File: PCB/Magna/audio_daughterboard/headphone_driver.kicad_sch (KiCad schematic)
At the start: 41 parts, among them J1201 AudioJack3, U1201 NE5532, U1202 NE5532, U1203 TDA2822D

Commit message: Some updates to PCB
Honestly I cannot remember whats changed
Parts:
- renumbered C1201 to C601, C1202 to C602, C1203 to C603, C1204 to C604, C1205 to C605, C1206 to C606, C1207 to C607, C1208 to C608, C1209 to C609, C1210 to C610, C1211 to C611, C1212 to C612, C1213 to C613, C1214 to C614, C1215 to C615, C1216 to C616, C1217 to C617, J1201 to J601, R1201 to R601, R1202 to R602, R1203 to R603, R1204 to R604, R1205 to R605, R1206 to R606, R1207 to R607, R1208 to R608, R1209 to R609, R1210 to R610, R1211 to R611, R1212 to R612, R1213 to R613, R1214 to R614, RV1201 to RV601, TP1201 to TP601, TP1202 to TP602, TP1203 to TP603, TP1204 to TP604, TP1205 to TP605, U1201 to U601, U1202 to U602, U1203 to U603

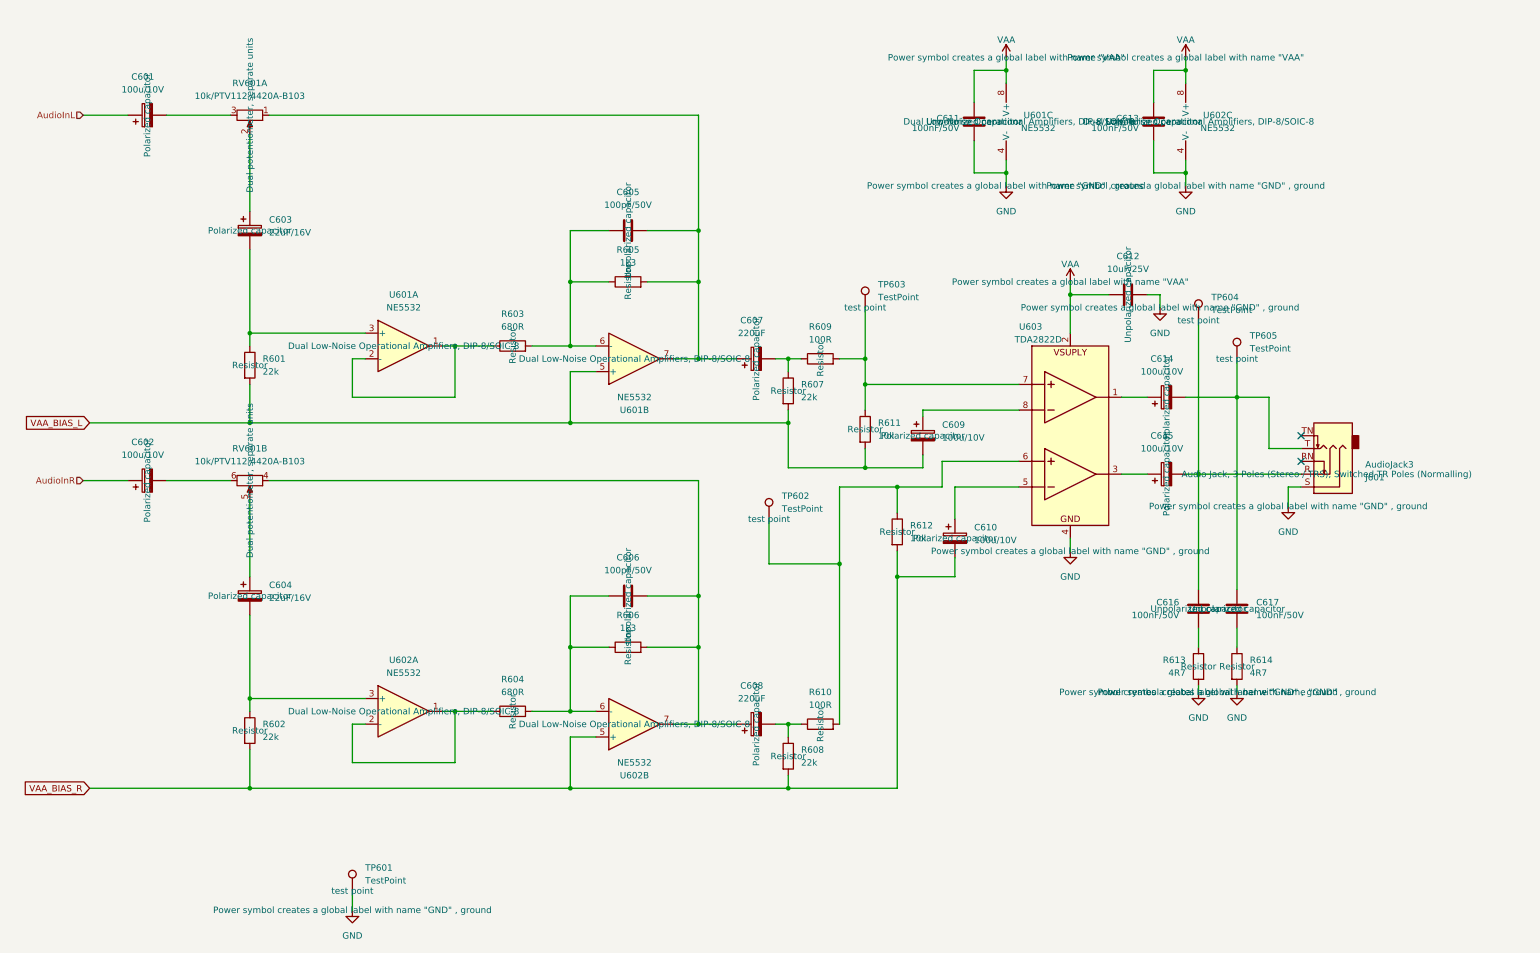
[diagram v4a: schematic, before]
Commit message: Update schematics to Kicad 9
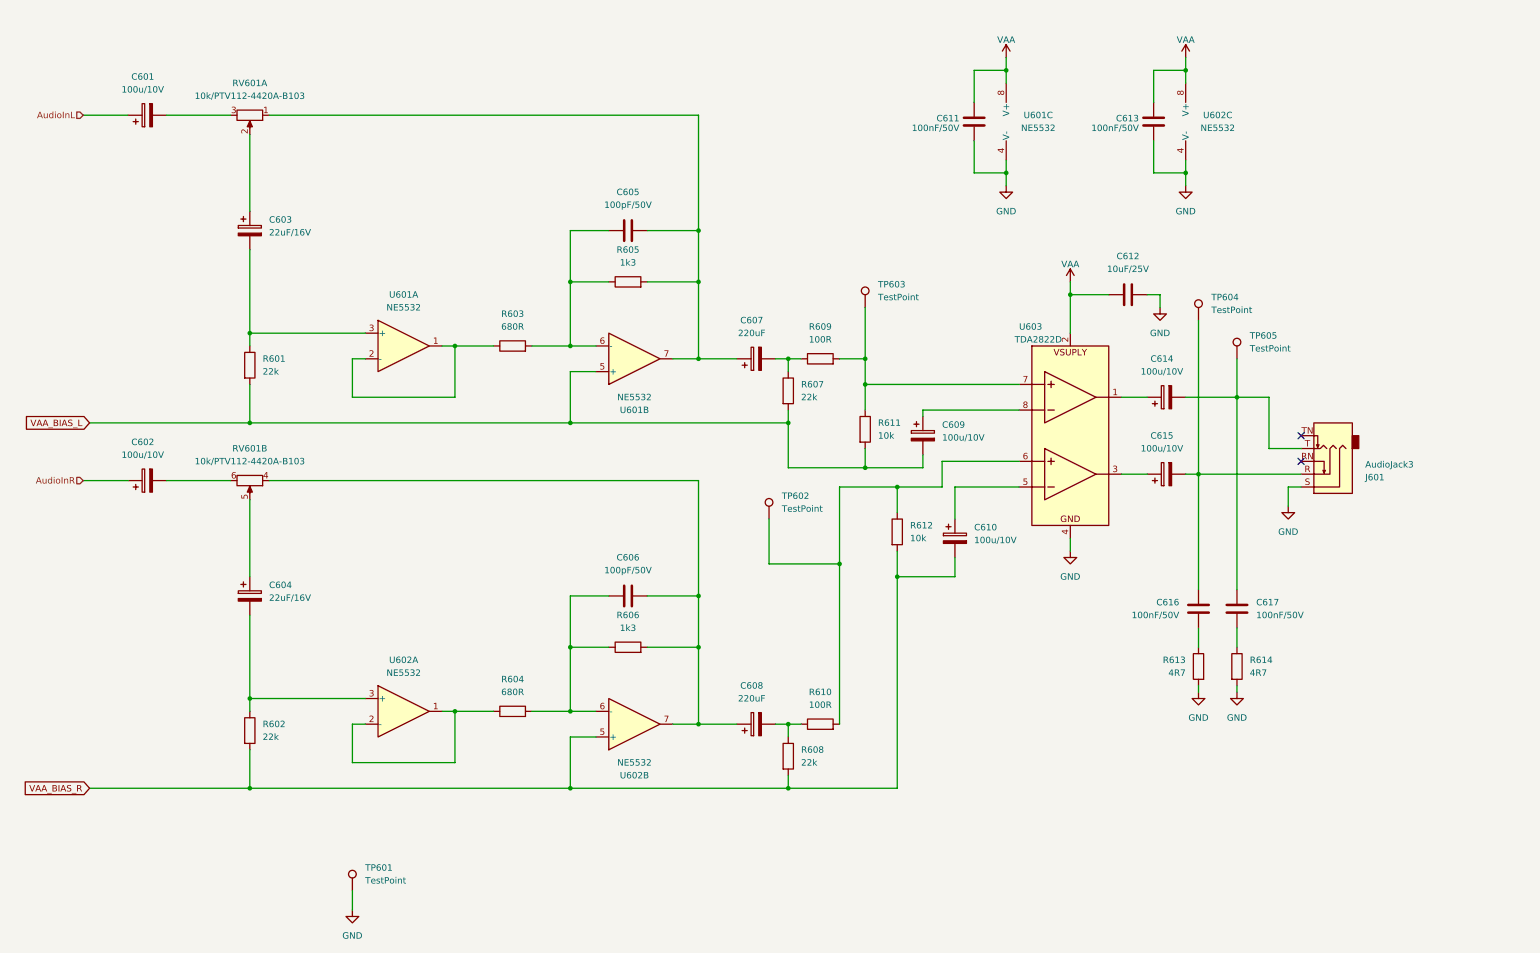
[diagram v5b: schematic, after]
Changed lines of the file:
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@@
 					(size 1.27 1.27)
 				)
+				(hide yes)
 			)
 		)
@@
 					(size 1.27 1.27)
 				)
+				(hide yes)
 			)
 		)
@@
 					(size 1.27 1.27)
 				)
+				(hide yes)
 			)
 		)
@@
 					(size 1.27 1.27)
 				)
+				(hide yes)
 			)
 		)
@@
 					(size 1.27 1.27)
 				)
+				(hide yes)
 			)
 		)
@@
 					(size 1.27 1.27)
 				)
+				(hide yes)
 			)
 		)
@@
 					(size 1.27 1.27)
 				)
+				(hide yes)
 			)
 		)
@@
 					(size 1.27 1.27)
 				)
+				(hide yes)
 			)
 		)
@@
 					(size 1.27 1.27)
 				)
+				(hide yes)
 			)
 		)
@@
 					(size 1.27 1.27)
 				)
+				(hide yes)
 			)
 		)
@@
 					(size 1.27 1.27)
 				)
+				(hide yes)
 			)
 		)
@@
 					(size 1.27 1.27)
 				)
+				(hide yes)
 			)
 		)
@@
 					(size 1.27 1.27)
 				)
+				(hide yes)
 			)
 		)
@@
 					(size 1.27 1.27)
 				)
+				(hide yes)
 			)
 		)
@@
 					(size 1.27 1.27)
 				)
+				(hide yes)
 			)
 		)
@@
 					(size 1.27 1.27)
 				)
+				(hide yes)
 			)
 		)
@@
 					(size 1.27 1.27)
 				)
+				(hide yes)
 			)
 		)
@@
 					(size 1.27 1.27)
 				)
+				(hide yes)
 			)
 		)
@@
 					(size 1.27 1.27)
 				)
+				(hide yes)
 			)
 		)
@@
 					(size 1.27 1.27)
 				)
+				(hide yes)
 			)
 		)
@@
 					(size 1.27 1.27)
 				)
+				(hide yes)
 			)
 		)
@@
 					(size 1.27 1.27)
 				)
+				(hide yes)
 			)
 		)
@@
 					(size 1.27 1.27)
 				)
+				(hide yes)
 			)
 		)
@@
 					(size 1.27 1.27)
 				)
+				(hide yes)
 			)
 		)
@@
 					(size 1.27 1.27)
 				)
+				(hide yes)
 			)
 		)
@@
 					(size 1.27 1.27)
 				)
+				(hide yes)
 			)
 		)
@@
 					(size 1.27 1.27)
 				)
+				(hide yes)
 			)
 		)
@@
 					(size 1.27 1.27)
 				)
+				(hide yes)
 			)
 		)
@@
 					(size 1.27 1.27)
 				)
+				(hide yes)
 			)
 		)
@@
 					(size 1.27 1.27)
 				)
+				(hide yes)
 			)
 		)
@@
 					(size 1.27 1.27)
 				)
+				(hide yes)
 			)
 		)
@@
 					(size 1.27 1.27)
 				)
+				(hide yes)
 			)
 		)
@@
 					(size 1.27 1.27)
 				)
+				(hide yes)
 			)
 		)
@@
 					(size 1.27 1.27)
 				)
+				(hide yes)
 			)
 		)
@@
 					(size 1.27 1.27)
 				)
+				(hide yes)
 			)
 		)
@@
 					(size 1.27 1.27)
 				)
+				(hide yes)
 			)
 		)
@@
 					(size 1.27 1.27)
 				)
+				(hide yes)
 			)
 		)
@@
 					(size 1.27 1.27)
 				)
+				(hide yes)
 			)
 		)
@@
 					(size 1.27 1.27)
 				)
+				(hide yes)
 			)
 		)
@@
 					(size 1.27 1.27)
 				)
+				(hide yes)
 			)
 		)
@@
 					(size 1.27 1.27)
 				)
+				(hide yes)
 			)
 		)
@@
 					(size 1.27 1.27)
 				)
+				(hide yes)
 			)
 		)
@@
 					(size 1.27 1.27)
 				)
+				(hide yes)
 			)
 		)
@@
 					(size 1.27 1.27)
 				)
+				(hide yes)
 			)
 		)
@@
 					(size 1.27 1.27)
 				)
+				(hide yes)
 			)
 		)
@@
 					(size 1.27 1.27)
 				)
+				(hide yes)
 			)
 		)
@@
 					(size 1.27 1.27)
 				)
+				(hide yes)
 			)
 		)
@@
 					(size 1.27 1.27)
 				)
+				(hide yes)
 			)
 		)
@@
 					(size 1.27 1.27)
 				)
+				(hide yes)
 			)
 		)
@@
 					(size 1.27 1.27)
 				)
+				(hide yes)
 			)
 		)
@@
 					(size 1.27 1.27)
 				)
+				(hide yes)
 			)
 		)
@@
 					(size 1.27 1.27)
 				)
+				(hide yes)
 			)
 		)
@@
 					(size 1.27 1.27)
 				)
+				(hide yes)
 			)
 		)
@@
 					(size 1.27 1.27)
 				)
+				(hide yes)
 			)
 		)
@@
 					(size 1.27 1.27)
 				)
+				(hide yes)
 			)
 		)
@@
 					(size 1.27 1.27)
 				)
+				(hide yes)
 			)
 		)

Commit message: Update audio PCB
Mainly added simulations to Linedriver and DAC.

Also fixed some small issues that was found when simulating
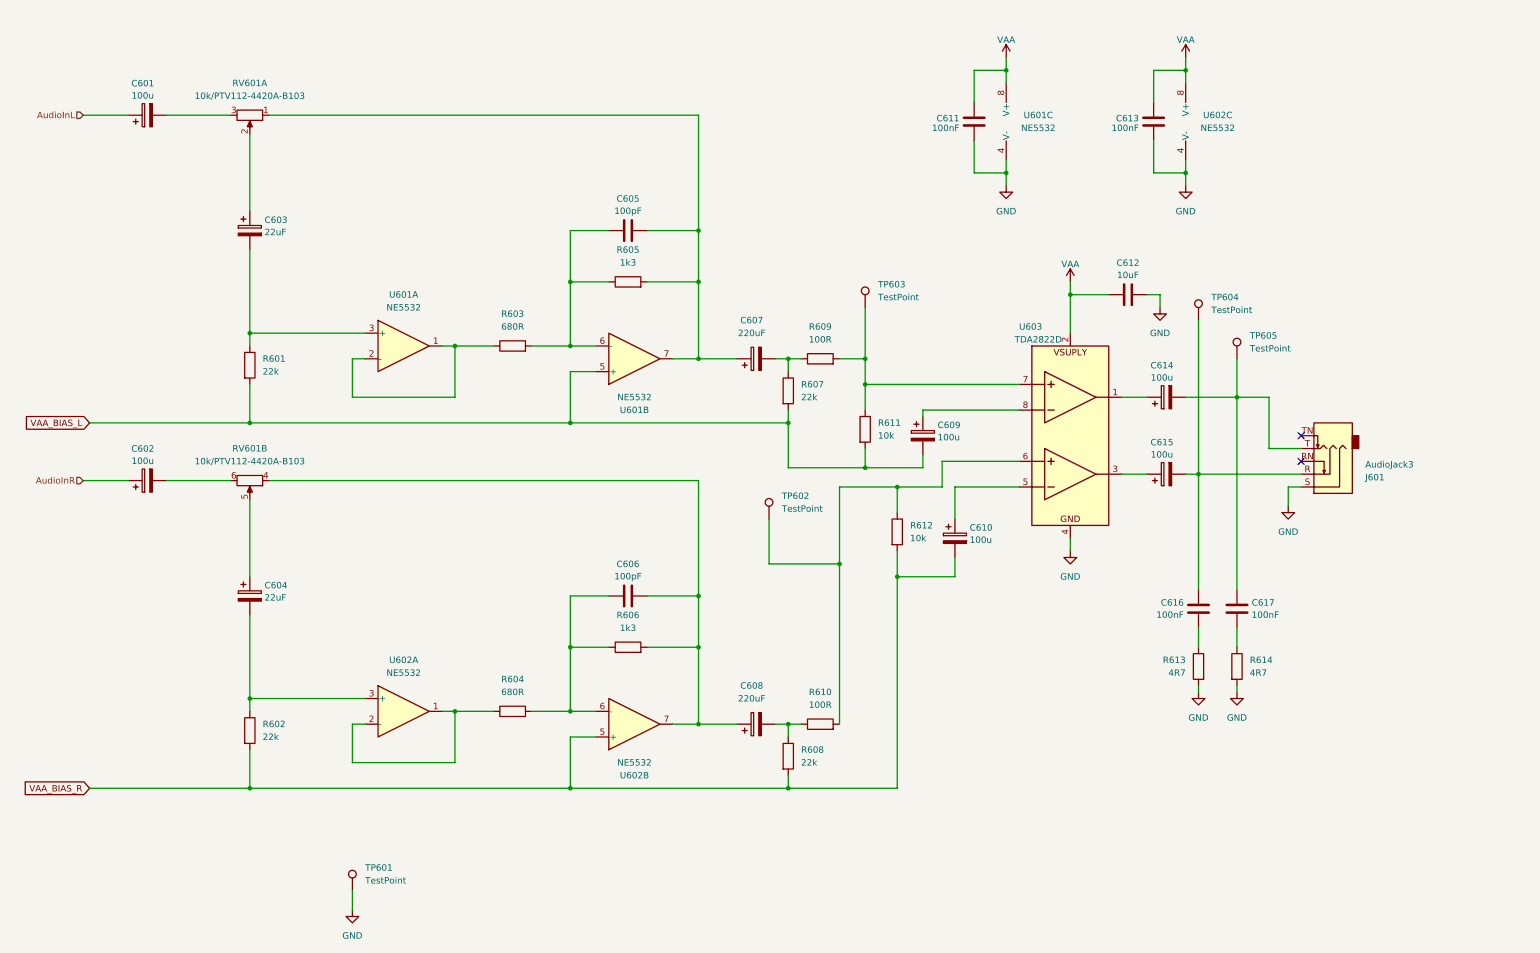
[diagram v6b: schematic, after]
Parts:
- C601, C602, C609, C610, C614, C615: value 100u/10V -> 100u
- C603, C604: value 22uF/16V -> 22uF
- C605, C606: value 100pF/50V -> 100pF
- C611, C613, C616, C617: value 100nF/50V -> 100nF
- C612: value 10uF/25V -> 10uF
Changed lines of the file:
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@@
 		(fields_autoplaced yes)
 		(property "Reference" "C610"
-			(at 201.93 114.681 0)
+			(at 201.041 114.7388 0)
 			(effects
 				(font
@@
 			)
 		)
-		(property "Value" "100u/10V"
-			(at 201.93 117.221 0)
+		(property "Value" "100u"
+			(at 201.041 117.1631 0)
 			(effects
 				(font
@@
 		(fields_autoplaced yes)
 		(property "Reference" "C609"
-			(at 195.58 94.361 0)
+			(at 194.691 94.4188 0)
 			(effects
 				(font
@@
 			)
 		)
-		(property "Value" "100u/10V"
-			(at 195.58 96.901 0)
+		(property "Value" "100u"
+			(at 194.691 96.8431 0)
 			(effects
 				(font
@@
 		(fields_autoplaced yes)
 		(property "Reference" "C612"
-			(at 232.41 60.96 90)
+			(at 232.41 62.2765 90)
 			(effects
 				(font
@@
 			)
 		)
-		(property "Value" "10uF/25V"
-			(at 232.41 63.5 90)
+		(property "Value" "10uF"
+			(at 232.41 64.7008 90)
 			(effects
 				(font
@@
 		(fields_autoplaced yes)
 		(property "Reference" "C605"
-			(at 133.35 48.26 90)
+			(at 133.35 49.5765 90)
 			(effects
 				(font
@@
 			)
 		)
-		(property "Value" "100pF/50V"
-			(at 133.35 50.8 90)
+		(property "Value" "100pF"
+			(at 133.35 52.0008 90)
 			(effects
 				(font
@@
 		(fields_autoplaced yes)
 		(property "Reference" "C604"
-			(at 62.23 126.111 0)
+			(at 61.341 126.1688 0)
 			(effects
 				(font
@@
 			)
 		)
-		(property "Value" "22uF/16V"
-			(at 62.23 128.651 0)
+		(property "Value" "22uF"
+			(at 61.341 128.5931 0)
 			(effects
 				(font
@@
 		(fields_autoplaced yes)
 		(property "Reference" "C606"
-			(at 133.35 120.65 90)
+			(at 133.35 121.9665 90)
 			(effects
 				(font
@@
 			)
 		)
-		(property "Value" "100pF/50V"
-			(at 133.35 123.19 90)
+		(property "Value" "100pF"
+			(at 133.35 124.3908 90)
 			(effects
 				(font
@@
 		(fields_autoplaced yes)
 		(property "Reference" "C615"
-			(at 239.141 96.52 90)
+			(at 239.141 97.8365 90)
 			(effects
 				(font
@@
 			)
 		)
-		(property "Value" "100u/10V"
-			(at 239.141 99.06 90)
+		(property "Value" "100u"
+			(at 239.141 100.2608 90)
 			(effects
 				(font
@@
 		(fields_autoplaced yes)
 		(property "Reference" "C614"
-			(at 239.141 81.28 90)
+			(at 239.141 82.5965 90)
 			(effects
 				(font
@@
 			)
 		)
-		(property "Value" "100u/10V"
-			(at 239.141 83.82 90)
+		(property "Value" "100u"
+			(at 239.141 85.0208 90)
 			(effects
 				(font
@@
 		(fields_autoplaced yes)
 		(property "Reference" "C602"
-			(at 37.211 97.79 90)
+			(at 37.211 99.1065 90)
 			(effects
 				(font
@@
 			)
 		)
-		(property "Value" "100u/10V"
-			(at 37.211 100.33 90)
+		(property "Value" "100u"
+			(at 37.211 101.5308 90)
 			(effects
 				(font
@@
 		(fields_autoplaced yes)
 		(property "Reference" "C616"
-			(at 242.57 129.54 0)
+			(at 243.4591 129.5978 0)
 			(effects
 				(font
@@
 			)
 		)
-		(property "Value" "100nF/50V"
-			(at 242.57 132.08 0)
+		(property "Value" "100nF"
+			(at 243.4591 132.0221 0)
 			(effects
 				(font
@@
 			)
 		)
-		(property "Value" "100nF/50V"
+		(property "Value" "100nF"
 			(at 199.009 35.5673 0)
 			(effects
@@
 		(fields_autoplaced yes)
 		(property "Reference" "C603"
-			(at 62.23 53.721 0)
+			(at 61.341 53.7788 0)
 			(effects
 				(font
@@
 			)
 		)
-		(property "Value" "22uF/16V"
-			(at 62.23 56.261 0)
+		(property "Value" "22uF"
+			(at 61.341 56.2031 0)
 			(effects
 				(font
@@
 		(fields_autoplaced yes)
 		(property "Reference" "C617"
-			(at 257.81 129.54 0)
+			(at 256.921 129.5978 0)
 			(effects
 				(font
@@
 			)
 		)
-		(property "Value" "100nF/50V"
-			(at 257.81 132.08 0)
+		(property "Value" "100nF"
+			(at 256.921 132.0221 0)
 			(effects
 				(font
@@
 		(fields_autoplaced yes)
 		(property "Reference" "C601"
-			(at 37.211 25.4 90)
+			(at 37.211 26.7165 90)
 			(effects
 				(font
@@
 			)
 		)
-		(property "Value" "100u/10V"
-			(at 37.211 27.94 90)
+		(property "Value" "100u"
+			(at 37.211 29.1408 90)
 			(effects
 				(font
@@
 			)
 		)
-		(property "Value" "100nF/50V"
+		(property "Value" "100nF"
 			(at 234.569 35.5673 0)
 			(effects
